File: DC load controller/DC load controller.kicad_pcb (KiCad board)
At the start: 2 copper layers, 45 x 25 mm, 21 parts, among them J1 Ctrl In, J2 Batt in, J3 Ctrl Out, J4 Pwr in, M1 3mm, M2 3mm, M3 3mm, U1 LM324

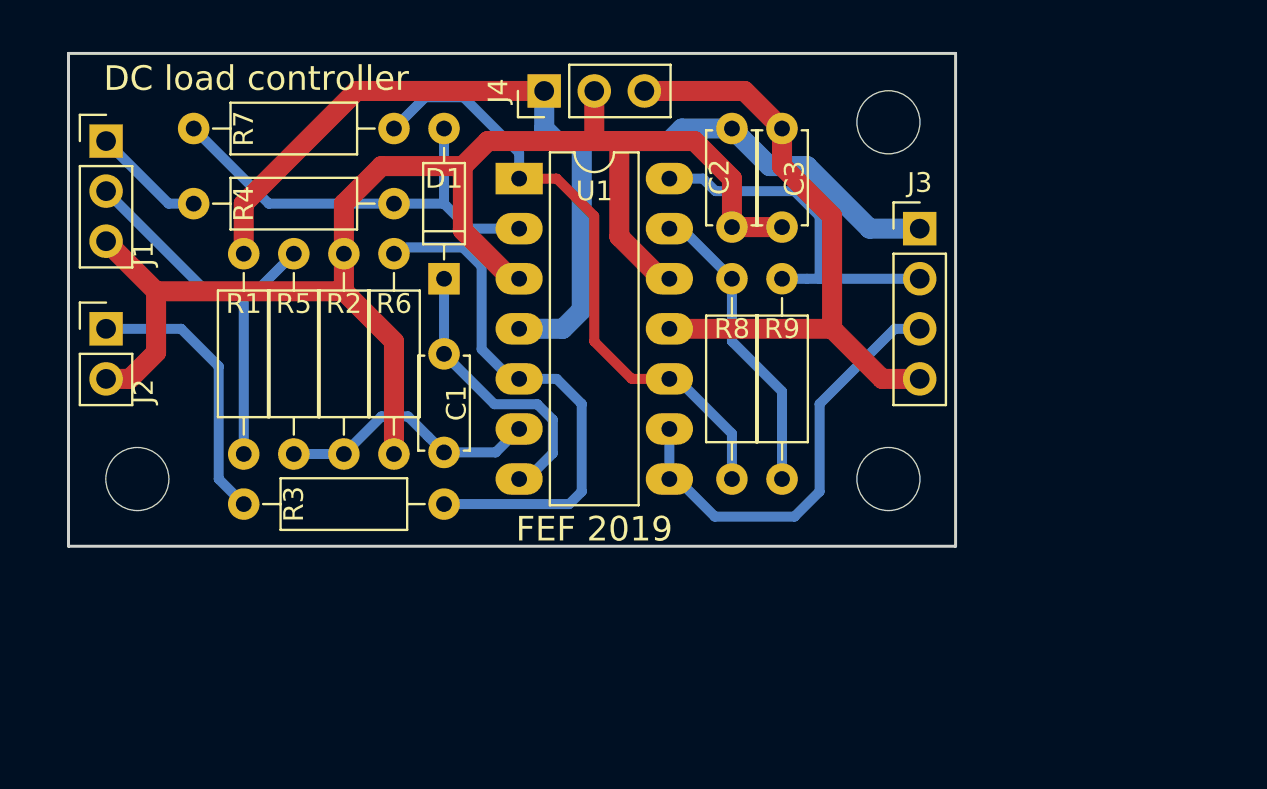
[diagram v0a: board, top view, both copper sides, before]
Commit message: Some stability and safety features added to controller
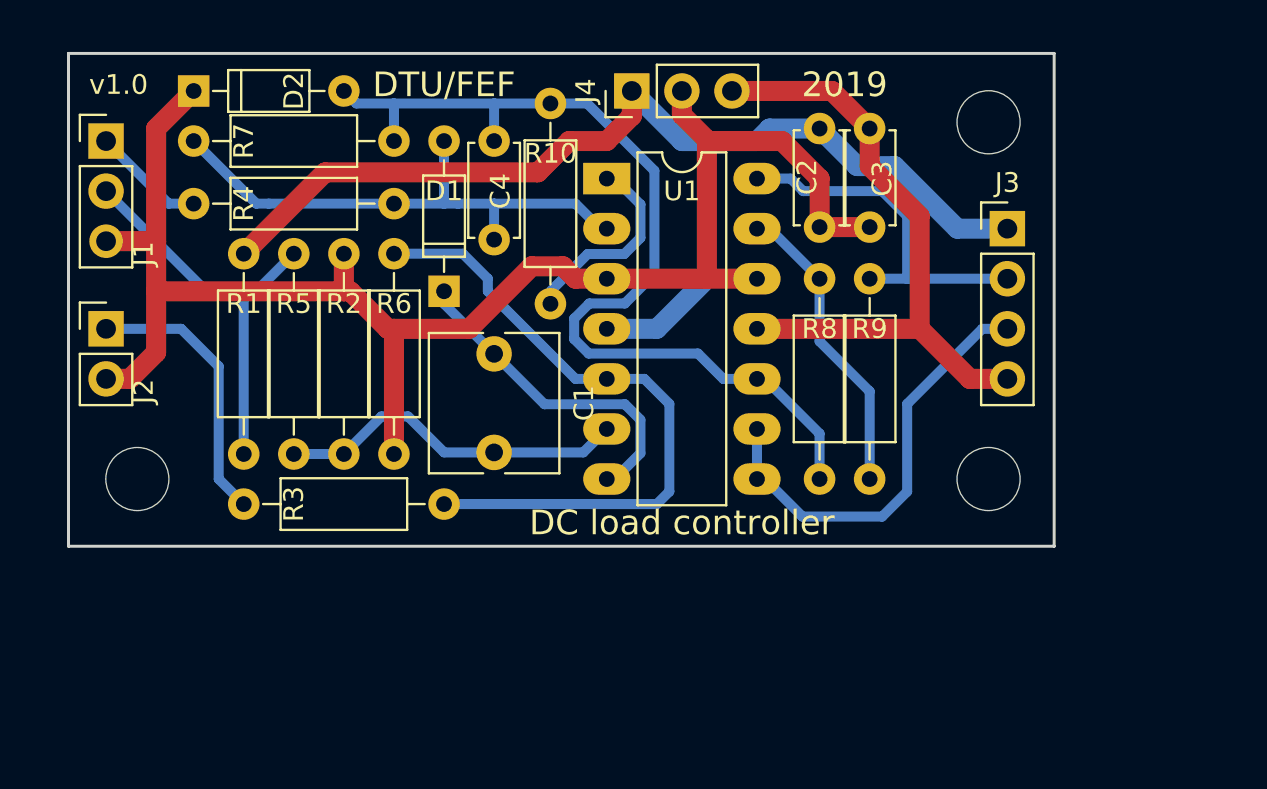
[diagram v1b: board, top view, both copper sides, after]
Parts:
- added C4: 10n, Capacitors_THT:C_Disc_D4.7mm_W2.5mm_P5.00mm, F.Cu at (123.2, 72.9)
- added D2: 5v6, Diodes_THT:D_DO-35_SOD27_P7.62mm_Horizontal, F.Cu at (108.0, 65.4)
- added R10: 953, Resistors_THT:R_Axial_DIN0207_L6.3mm_D2.5mm_P10.16mm_Horizontal, F.Cu at (126.0, 66.0)
- C1: value 470n -> 2u2; footprint Capacitors_THT:C_Disc_D4.7mm_W2.5mm_P5.00mm -> Capacitors_THT:C_Rect_L7.0mm_W6.5mm_P5.00mm
- R1: value 121k -> 66k5
- R2, R3: value 10k -> 20k
- R4: value 2k -> 20k
- R5, R6: value 1k -> 2k
- R7: value 1k -> 10k
- moved M2 5.08 mm to (148.3, 85.1)
- moved M3 5.08 mm to (148.3, 67.0)
- moved C3 4.45 mm to (142.2, 72.3)
- moved R9 4.45 mm to (142.2, 85.1)
- moved J4 4.45 mm to (130.2, 65.4)
- moved U1 4.45 mm to (128.9, 69.8)
- moved C2 4.44 mm to (139.7, 67.3)
- moved J3 4.44 mm to (149.2, 72.4)
- moved R8 4.44 mm to (139.7, 74.9)
- moved C1 2.54 mm to (123.2, 78.7)
- moved D1 0.63 mm to (120.7, 75.6)
- moved R7 0.63 mm to (118.1, 67.9)
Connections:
- R7 pad 1: Net-(R7-Pad1) -> Net-(C4-Pad2)
- R8 pad 2: Net-(R7-Pad1) -> Net-(C4-Pad2)
- U1 pad 1: Net-(R7-Pad1) -> Net-(R10-Pad2)
- U1 pad 10: Net-(R7-Pad1) -> Net-(C4-Pad2)
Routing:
- net Net-(C4-Pad2): track 0.00 -> 49.3 mm
- net Net-(R7-Pad1): track 31.7 -> 0.00 mm
- net Net-(R10-Pad2): track 0.00 -> 9.64 mm
- net Net-(R3-Pad1): track 27.1 -> 34.5 mm
- net Net-(C4-Pad1): track 22.2 -> 28.2 mm
- net GND: track 78.2 -> 83.2 mm
- net Net-(C1-Pad2): track 13.5 -> 18.0 mm
- net VDD: track 55.9 -> 59.4 mm
- net Net-(C1-Pad1): track 14.7 -> 17.0 mm
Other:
- board size 45 x 25 mm -> 50 x 25 mm
- board text added: "2019"
- board text added: "DTU/FEF"
- board text added: "v1.0"
- board text removed: "FEF 2019"

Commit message: New opamp selection for load controller (700mA output drive for controlling many loads)
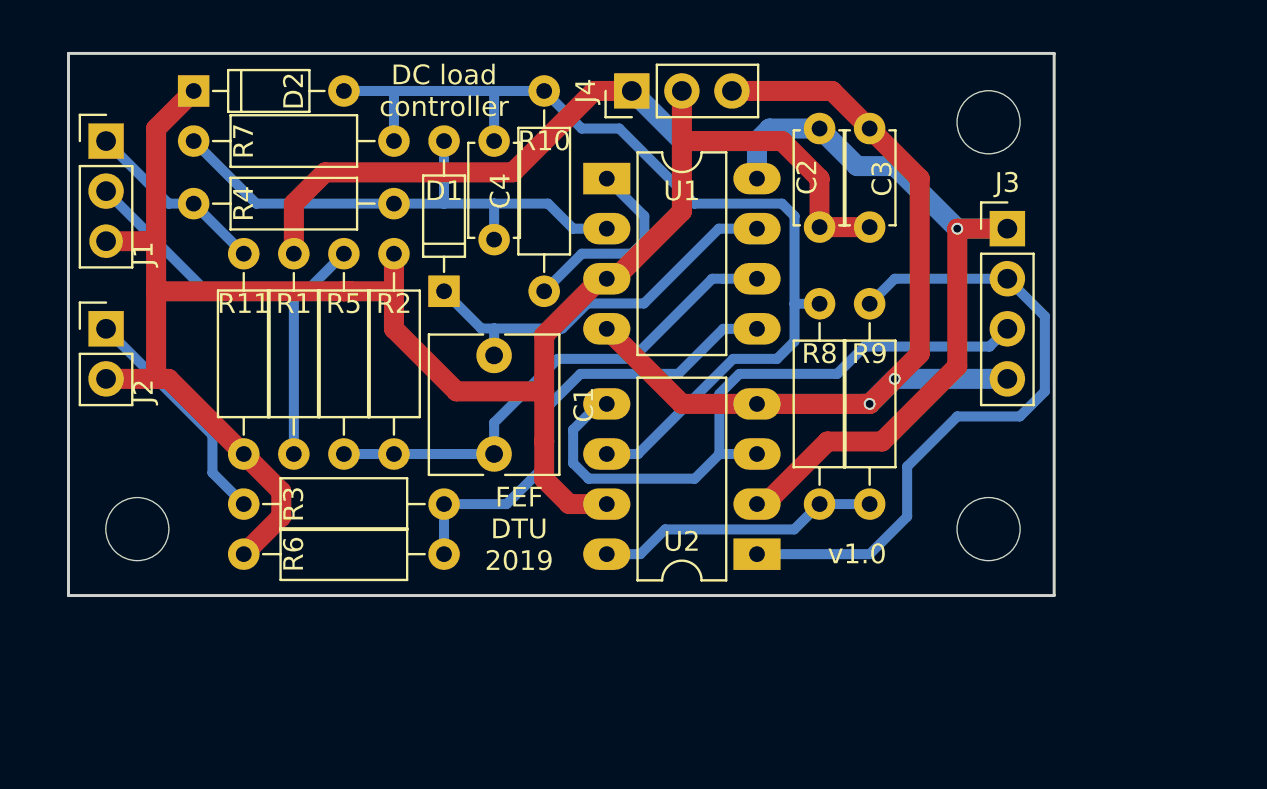
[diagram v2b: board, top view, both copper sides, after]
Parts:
- added R11: 1k, Resistors_THT:R_Axial_DIN0207_L6.3mm_D2.5mm_P10.16mm_Horizontal, F.Cu at (110.5, 73.7)
- added U2: L272AM, Housings_DIP:DIP-8_W7.62mm_LongPads, F.Cu at (136.5, 88.9)
- U1: value LM324 -> LM358; footprint Housings_DIP:DIP-14_W7.62mm_LongPads -> Housings_DIP:DIP-8_W7.62mm_LongPads
- moved R6 15.5 mm to (120.7, 88.9), turned to 180 degrees
- moved R8 11.4 mm to (139.7, 86.4), turned to 90 degrees
- moved R1 2.54 mm to (113.0, 73.7)
- moved R5 2.54 mm to (118.1, 83.8)
- moved M1 2.54 mm to (105.1, 87.6)
- moved M2 2.54 mm to (148.3, 87.6)
- moved R2 2.54 mm to (115.6, 73.7)
- moved R9 1.27 mm to (142.2, 86.4)
- moved R10 0.71 mm to (125.7, 65.4)
- moved C1 0.08 mm to (123.2, 78.8)
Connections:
- U1 pad 4: VDD -> VSS
- U1 pad 8: Net-(J3-Pad3) -> VDD
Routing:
- net VSS: track 32.7 -> 52.4 mm, vias 0 -> 2
- net GND: track 83.2 -> 97.8 mm
- net Net-(J3-Pad2): track 19.4 -> 33.5 mm
- net Net-(R3-Pad1): track 34.5 -> 23.8 mm
- net Net-(J3-Pad3): track 23.0 -> 33.5 mm
- net VDD: track 59.4 -> 69.0 mm, vias 0 -> 1
- net Net-(C1-Pad2): track 18.0 -> 26.0 mm
- net Net-(J1-Pad1): track 5.76 -> 9.35 mm
- net Net-(C1-Pad1): track 17.0 -> 20.1 mm
- net Net-(J1-Pad2): track 20.7 -> 23.2 mm
- net Net-(J2-Pad1): track 14.0 -> 11.8 mm
- net Net-(R8-Pad1): track 15.4 -> 14.4 mm
- net Net-(C4-Pad2): track 49.3 -> 50.1 mm
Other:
- board size 50 x 25 mm -> 50 x 27.5 mm
- board text added: "FEF DTU 2019"
- board text removed: "2019"
- board text removed: "DTU/FEF"

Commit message: L272A prototype 2 (first was unstable)
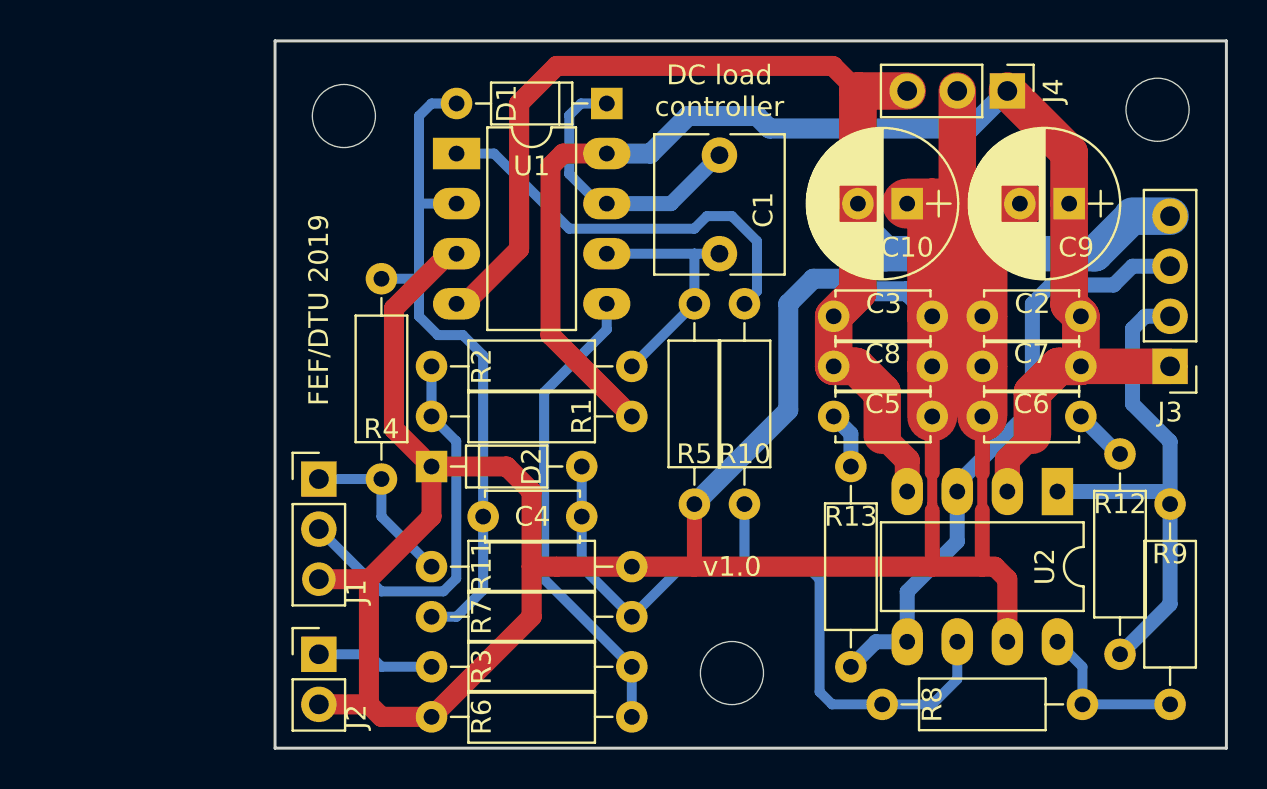
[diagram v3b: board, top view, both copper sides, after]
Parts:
- added C10: 47u, Capacitors_THT:CP_Radial_D7.5mm_P2.50mm, F.Cu at (144.1, 71.1)
- added C5: 100n, Capacitors_THT:C_Disc_D4.7mm_W2.5mm_P5.00mm, F.Cu at (140.4, 81.9)
- added C6: 100n, Capacitors_THT:C_Disc_D4.7mm_W2.5mm_P5.00mm, F.Cu at (153.0, 81.9)
- added C7: 10n, Capacitors_THT:C_Disc_D4.7mm_W2.5mm_P5.00mm, F.Cu at (153.0, 79.4)
- added C8: 10n, Capacitors_THT:C_Disc_D4.7mm_W2.5mm_P5.00mm, F.Cu at (145.4, 79.4)
- added C9: 47u, Capacitors_THT:CP_Radial_D7.5mm_P2.50mm, F.Cu at (152.4, 71.1)
- added R12: 1R0, Resistors_THT:R_Axial_DIN0207_L6.3mm_D2.5mm_P10.16mm_Horizontal, F.Cu at (154.9, 83.8)
- added R13: 1R0, Resistors_THT:R_Axial_DIN0207_L6.3mm_D2.5mm_P10.16mm_Horizontal, F.Cu at (141.3, 84.5)
- C2, C3: value 100n -> 220n
- moved M2 38.8 mm to (115.6, 66.7)
- moved M1 31.0 mm to (135.3, 94.9)
- moved R7 27.0 mm to (130.2, 92.1)
- moved R10 23.3 mm to (135.9, 86.4), turned to 90 degrees
- moved D2 22.5 mm to (120.0, 84.5)
- moved J1 20.3 mm to (114.3, 85.1)
- moved J2 19.7 mm to (114.3, 94.0)
- moved J4 19.0 mm to (149.2, 65.4), turned to 270 degrees
- moved R1 19.0 mm to (130.2, 81.9), turned to 180 degrees
- moved R11 18.5 mm to (120.0, 89.5), turned to 0 degrees
- moved R9 18.3 mm to (157.5, 96.5)
- moved R5 17.0 mm to (133.3, 76.2), turned to 270 degrees
- moved R8 16.8 mm to (153.0, 96.5), turned to 180 degrees
- moved C2 16.3 mm to (153.0, 76.8), turned to 180 degrees
- moved U2 15.6 mm to (151.8, 85.7), turned to 270 degrees
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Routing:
- net GND: track 97.8 -> 153.9 mm
- net VSS: track 52.4 -> 74.1 mm, vias 2 -> 0
- net Net-(C1-Pad2): track 26.0 -> 12.7 mm
- net Net-(C4-Pad2): track 50.1 -> 38.1 mm
- net Net-(R10-Pad2): track 10.1 -> 21.0 mm
- net Net-(C4-Pad1): track 27.8 -> 35.7 mm
- net Net-(J3-Pad2): track 33.5 -> 26.2 mm
- net Net-(R8-Pad1): track 14.4 -> 8.15 mm
- net Net-(J2-Pad1): track 11.8 -> 5.98 mm
- net Net-(C1-Pad1): track 20.1 -> 14.4 mm
- net Net-(J1-Pad2): track 23.2 -> 19.8 mm
- net Net-(C5-Pad1): track 0.00 -> 2.90 mm
- net Net-(C6-Pad1): track 0.00 -> 2.77 mm
- net Net-(J3-Pad3): track 33.5 -> 30.9 mm
- net VDD: track 69.0 -> 68.3 mm, vias 1 -> 0
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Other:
- board size 50 x 27.5 mm -> 48.3 x 35.9 mm
- board text added: "FEF/DTU 2019"
- board text removed: "FEF DTU 2019"
